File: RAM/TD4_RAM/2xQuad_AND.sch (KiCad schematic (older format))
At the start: 2 parts, among them U4 74HC21

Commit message: RAM done (damn buses\!)
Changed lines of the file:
@@
 $Descr A4 11693 8268
 encoding utf-8
-Sheet 5 46
+Sheet 5 47
 Title ""
 Date ""
@@
 P 4950 2500
 AR Path="/5C5DC05E/5C84D72F/5C84D8AE" Ref="U4"  Part="1"
-AR Path="/5C5DC05E/5C8E8F76/5C84D8AE" Ref="U20"  Part="1"
-AR Path="/5C5DC05E/5C8E8F7D/5C84D8AE" Ref="U21"  Part="1"
-AR Path="/5C5DC05E/5C8E8F84/5C84D8AE" Ref="U29"  Part="1"
-AR Path="/5C5DC05E/5C8E8FA2/5C84D8AE" Ref="U28"  Part="1"
-AR Path="/5C5DC05E/5C8E8FA8/5C84D8AE" Ref="U22"  Part="1"
-AR Path="/5C5DC05E/5C8E8FAE/5C84D8AE" Ref="U23"  Part="1"
-AR Path="/5C5DC05E/5C8E8FB4/5C84D8AE" Ref="U24"  Part="1"
-F 0 "U29" H 4950 2875 50  0000 C CNN
+AR Path="/5C5DC05E/5C8E8F76/5C84D8AE" Ref="U?"  Part="1"
+AR Path="/5C5DC05E/5C8E8F7D/5C84D8AE" Ref="U?"  Part="1"
+AR Path="/5C5DC05E/5C8E8F84/5C84D8AE" Ref="U?"  Part="1"
+AR Path="/5C5DC05E/5C8E8FA2/5C84D8AE" Ref="U?"  Part="1"
+AR Path="/5C5DC05E/5C8E8FA8/5C84D8AE" Ref="U?"  Part="1"
+AR Path="/5C5DC05E/5C8E8FAE/5C84D8AE" Ref="U?"  Part="1"
+AR Path="/5C5DC05E/5C8E8FB4/5C84D8AE" Ref="U?"  Part="1"
+AR Path="/5C5DC05E/5CD2847D/5C84D8AE" Ref="U35"  Part="1"
+AR Path="/5C5DC05E/5CD2F166/5C84D8AE" Ref="U36"  Part="1"
+AR Path="/5C5DC05E/5CD35E4F/5C84D8AE" Ref="U37"  Part="1"
+AR Path="/5C5DC05E/5CD3CB4F/5C84D8AE" Ref="U38"  Part="1"
+AR Path="/5C5DC05E/5CD3CB55/5C84D8AE" Ref="U39"  Part="1"
+AR Path="/5C5DC05E/5CD3CB5B/5C84D8AE" Ref="U40"  Part="1"
+AR Path="/5C5DC05E/5CD3CB61/5C84D8AE" Ref="U41"  Part="1"
+F 0 "U4" H 4950 2875 50  0000 C CNN
 F 1 "74HC21" H 4950 2784 50  0000 C CNN
 F 2 "" H 4950 2500 50  0001 C CNN
@@
 P 4950 3550
 AR Path="/5C5DC05E/5C84D72F/5C84D8EE" Ref="U4"  Part="2"
-AR Path="/5C5DC05E/5C8E8F76/5C84D8EE" Ref="U20"  Part="2"
-AR Path="/5C5DC05E/5C8E8F7D/5C84D8EE" Ref="U21"  Part="2"
-AR Path="/5C5DC05E/5C8E8F84/5C84D8EE" Ref="U29"  Part="2"
-AR Path="/5C5DC05E/5C8E8FA2/5C84D8EE" Ref="U28"  Part="2"
-AR Path="/5C5DC05E/5C8E8FA8/5C84D8EE" Ref="U22"  Part="2"
-AR Path="/5C5DC05E/5C8E8FAE/5C84D8EE" Ref="U23"  Part="2"
-AR Path="/5C5DC05E/5C8E8FB4/5C84D8EE" Ref="U24"  Part="2"
-F 0 "U29" H 4950 3925 50  0000 C CNN
+AR Path="/5C5DC05E/5C8E8F76/5C84D8EE" Ref="U?"  Part="2"
+AR Path="/5C5DC05E/5C8E8F7D/5C84D8EE" Ref="U?"  Part="2"
+AR Path="/5C5DC05E/5C8E8F84/5C84D8EE" Ref="U?"  Part="2"
+AR Path="/5C5DC05E/5C8E8FA2/5C84D8EE" Ref="U?"  Part="2"
+AR Path="/5C5DC05E/5C8E8FA8/5C84D8EE" Ref="U?"  Part="2"
+AR Path="/5C5DC05E/5C8E8FAE/5C84D8EE" Ref="U?"  Part="2"
+AR Path="/5C5DC05E/5C8E8FB4/5C84D8EE" Ref="U?"  Part="2"
+AR Path="/5C5DC05E/5CD2847D/5C84D8EE" Ref="U35"  Part="2"
+AR Path="/5C5DC05E/5CD2F166/5C84D8EE" Ref="U36"  Part="2"
+AR Path="/5C5DC05E/5CD35E4F/5C84D8EE" Ref="U37"  Part="2"
+AR Path="/5C5DC05E/5CD3CB4F/5C84D8EE" Ref="U38"  Part="2"
+AR Path="/5C5DC05E/5CD3CB55/5C84D8EE" Ref="U39"  Part="2"
+AR Path="/5C5DC05E/5CD3CB5B/5C84D8EE" Ref="U40"  Part="2"
+AR Path="/5C5DC05E/5CD3CB61/5C84D8EE" Ref="U41"  Part="2"
+F 0 "U4" H 4950 3925 50  0000 C CNN
 F 1 "74HC21" H 4950 3834 50  0000 C CNN
 F 2 "" H 4950 3550 50  0001 C CNN
@@
 P 8050 5500
 AR Path="/5C5DC05E/5C84D72F/5C84D959" Ref="U4"  Part="3"
-AR Path="/5C5DC05E/5C8E8F76/5C84D959" Ref="U20"  Part="3"
-AR Path="/5C5DC05E/5C8E8F7D/5C84D959" Ref="U21"  Part="3"
-AR Path="/5C5DC05E/5C8E8F84/5C84D959" Ref="U29"  Part="3"
-AR Path="/5C5DC05E/5C8E8FA2/5C84D959" Ref="U28"  Part="3"
-AR Path="/5C5DC05E/5C8E8FA8/5C84D959" Ref="U22"  Part="3"
-AR Path="/5C5DC05E/5C8E8FAE/5C84D959" Ref="U23"  Part="3"
-AR Path="/5C5DC05E/5C8E8FB4/5C84D959" Ref="U24"  Part="3"
-F 0 "U29" H 8280 5546 50  0000 L CNN
+AR Path="/5C5DC05E/5C8E8F76/5C84D959" Ref="U?"  Part="3"
+AR Path="/5C5DC05E/5C8E8F7D/5C84D959" Ref="U?"  Part="3"
+AR Path="/5C5DC05E/5C8E8F84/5C84D959" Ref="U?"  Part="3"
+AR Path="/5C5DC05E/5C8E8FA2/5C84D959" Ref="U?"  Part="3"
+AR Path="/5C5DC05E/5C8E8FA8/5C84D959" Ref="U?"  Part="3"
+AR Path="/5C5DC05E/5C8E8FAE/5C84D959" Ref="U?"  Part="3"
+AR Path="/5C5DC05E/5C8E8FB4/5C84D959" Ref="U?"  Part="3"
+AR Path="/5C5DC05E/5CD2847D/5C84D959" Ref="U35"  Part="3"
+AR Path="/5C5DC05E/5CD2F166/5C84D959" Ref="U36"  Part="3"
+AR Path="/5C5DC05E/5CD35E4F/5C84D959" Ref="U37"  Part="3"
+AR Path="/5C5DC05E/5CD3CB4F/5C84D959" Ref="U38"  Part="3"
+AR Path="/5C5DC05E/5CD3CB55/5C84D959" Ref="U39"  Part="3"
+AR Path="/5C5DC05E/5CD3CB5B/5C84D959" Ref="U40"  Part="3"
+AR Path="/5C5DC05E/5CD3CB61/5C84D959" Ref="U41"  Part="3"
+F 0 "U4" H 8280 5546 50  0000 L CNN
 F 1 "74HC21" H 8280 5455 50  0000 L CNN
 F 2 "" H 8050 5500 50  0001 C CNN
@@
 P 8700 5500
 AR Path="/5C5DC05E/5C84D72F/5C84DA33" Ref="C3"  Part="1"
-AR Path="/5C5DC05E/5C8E8F76/5C84DA33" Ref="C19"  Part="1"
-AR Path="/5C5DC05E/5C8E8F7D/5C84DA33" Ref="C20"  Part="1"
-AR Path="/5C5DC05E/5C8E8F84/5C84DA33" Ref="C28"  Part="1"
-AR Path="/5C5DC05E/5C8E8FA2/5C84DA33" Ref="C27"  Part="1"
-AR Path="/5C5DC05E/5C8E8FA8/5C84DA33" Ref="C21"  Part="1"
-AR Path="/5C5DC05E/5C8E8FAE/5C84DA33" Ref="C22"  Part="1"
-AR Path="/5C5DC05E/5C8E8FB4/5C84DA33" Ref="C23"  Part="1"
-F 0 "C28" H 8815 5546 50  0000 L CNN
+AR Path="/5C5DC05E/5C8E8F76/5C84DA33" Ref="C?"  Part="1"
+AR Path="/5C5DC05E/5C8E8F7D/5C84DA33" Ref="C?"  Part="1"
+AR Path="/5C5DC05E/5C8E8F84/5C84DA33" Ref="C?"  Part="1"
+AR Path="/5C5DC05E/5C8E8FA2/5C84DA33" Ref="C?"  Part="1"
+AR Path="/5C5DC05E/5C8E8FA8/5C84DA33" Ref="C?"  Part="1"
+AR Path="/5C5DC05E/5C8E8FAE/5C84DA33" Ref="C?"  Part="1"
+AR Path="/5C5DC05E/5C8E8FB4/5C84DA33" Ref="C?"  Part="1"
+AR Path="/5C5DC05E/5CD2847D/5C84DA33" Ref="C34"  Part="1"
+AR Path="/5C5DC05E/5CD2F166/5C84DA33" Ref="C35"  Part="1"
+AR Path="/5C5DC05E/5CD35E4F/5C84DA33" Ref="C36"  Part="1"
+AR Path="/5C5DC05E/5CD3CB4F/5C84DA33" Ref="C37"  Part="1"
+AR Path="/5C5DC05E/5CD3CB55/5C84DA33" Ref="C38"  Part="1"
+AR Path="/5C5DC05E/5CD3CB5B/5C84DA33" Ref="C39"  Part="1"
+AR Path="/5C5DC05E/5CD3CB61/5C84DA33" Ref="C40"  Part="1"
+F 0 "C3" H 8815 5546 50  0000 L CNN
 F 1 "100n" H 8815 5455 50  0000 L CNN
 F 2 "" H 8738 5350 50  0001 C CNN
@@
 	8700 5650 8700 6100
 $Comp
-L power:GND #PWR012
+L power:GND #PWR010
 U 1 1 5C84DB98
 P 8400 6100
-AR Path="/5C5DC05E/5C84D72F/5C84DB98" Ref="#PWR012"  Part="1"
-AR Path="/5C5DC05E/5C8E8F76/5C84DB98" Ref="#PWR074"  Part="1"
-AR Path="/5C5DC05E/5C8E8F7D/5C84DB98" Ref="#PWR076"  Part="1"
-AR Path="/5C5DC05E/5C8E8F84/5C84DB98" Ref="#PWR089"  Part="1"
-AR Path="/5C5DC05E/5C8E8FA2/5C84DB98" Ref="#PWR087"  Part="1"
-AR Path="/5C5DC05E/5C8E8FA8/5C84DB98" Ref="#PWR078"  Part="1"
-AR Path="/5C5DC05E/5C8E8FAE/5C84DB98" Ref="#PWR080"  Part="1"
-AR Path="/5C5DC05E/5C8E8FB4/5C84DB98" Ref="#PWR082"  Part="1"
-F 0 "#PWR089" H 8400 5850 50  0001 C CNN
+AR Path="/5C5DC05E/5C84D72F/5C84DB98" Ref="#PWR010"  Part="1"
+AR Path="/5C5DC05E/5C8E8F76/5C84DB98" Ref="#PWR?"  Part="1"
+AR Path="/5C5DC05E/5C8E8F7D/5C84DB98" Ref="#PWR?"  Part="1"
+AR Path="/5C5DC05E/5C8E8F84/5C84DB98" Ref="#PWR?"  Part="1"
+AR Path="/5C5DC05E/5C8E8FA2/5C84DB98" Ref="#PWR?"  Part="1"
+AR Path="/5C5DC05E/5C8E8FA8/5C84DB98" Ref="#PWR?"  Part="1"
+AR Path="/5C5DC05E/5C8E8FAE/5C84DB98" Ref="#PWR?"  Part="1"
+AR Path="/5C5DC05E/5C8E8FB4/5C84DB98" Ref="#PWR?"  Part="1"
+AR Path="/5C5DC05E/5CD2847D/5C84DB98" Ref="#PWR0132"  Part="1"
+AR Path="/5C5DC05E/5CD2F166/5C84DB98" Ref="#PWR0134"  Part="1"
+AR Path="/5C5DC05E/5CD35E4F/5C84DB98" Ref="#PWR0136"  Part="1"
+AR Path="/5C5DC05E/5CD3CB4F/5C84DB98" Ref="#PWR0138"  Part="1"
+AR Path="/5C5DC05E/5CD3CB55/5C84DB98" Ref="#PWR0140"  Part="1"
+AR Path="/5C5DC05E/5CD3CB5B/5C84DB98" Ref="#PWR0142"  Part="1"
+AR Path="/5C5DC05E/5CD3CB61/5C84DB98" Ref="#PWR0144"  Part="1"
+F 0 "#PWR0144" H 8400 5850 50  0001 C CNN
 F 1 "GND" H 8405 5927 50  0000 C CNN
 F 2 "" H 8400 6100 50  0001 C CNN
@@
 	8400 6100 8700 6100
 $Comp
-L power:VCC #PWR011
+L power:VCC #PWR09
 U 1 1 5C84DC2A
 P 8400 4900
-AR Path="/5C5DC05E/5C84D72F/5C84DC2A" Ref="#PWR011"  Part="1"
-AR Path="/5C5DC05E/5C8E8F76/5C84DC2A" Ref="#PWR073"  Part="1"
-AR Path="/5C5DC05E/5C8E8F7D/5C84DC2A" Ref="#PWR075"  Part="1"
-AR Path="/5C5DC05E/5C8E8F84/5C84DC2A" Ref="#PWR088"  Part="1"
-AR Path="/5C5DC05E/5C8E8FA2/5C84DC2A" Ref="#PWR086"  Part="1"
-AR Path="/5C5DC05E/5C8E8FA8/5C84DC2A" Ref="#PWR077"  Part="1"
-AR Path="/5C5DC05E/5C8E8FAE/5C84DC2A" Ref="#PWR079"  Part="1"
-AR Path="/5C5DC05E/5C8E8FB4/5C84DC2A" Ref="#PWR081"  Part="1"
-F 0 "#PWR088" H 8400 4750 50  0001 C CNN
+AR Path="/5C5DC05E/5C84D72F/5C84DC2A" Ref="#PWR09"  Part="1"
+AR Path="/5C5DC05E/5C8E8F76/5C84DC2A" Ref="#PWR?"  Part="1"
+AR Path="/5C5DC05E/5C8E8F7D/5C84DC2A" Ref="#PWR?"  Part="1"
+AR Path="/5C5DC05E/5C8E8F84/5C84DC2A" Ref="#PWR?"  Part="1"
+AR Path="/5C5DC05E/5C8E8FA2/5C84DC2A" Ref="#PWR?"  Part="1"
+AR Path="/5C5DC05E/5C8E8FA8/5C84DC2A" Ref="#PWR?"  Part="1"
+AR Path="/5C5DC05E/5C8E8FAE/5C84DC2A" Ref="#PWR?"  Part="1"
+AR Path="/5C5DC05E/5C8E8FB4/5C84DC2A" Ref="#PWR?"  Part="1"
+AR Path="/5C5DC05E/5CD2847D/5C84DC2A" Ref="#PWR0131"  Part="1"
+AR Path="/5C5DC05E/5CD2F166/5C84DC2A" Ref="#PWR0133"  Part="1"
+AR Path="/5C5DC05E/5CD35E4F/5C84DC2A" Ref="#PWR0135"  Part="1"
+AR Path="/5C5DC05E/5CD3CB4F/5C84DC2A" Ref="#PWR0137"  Part="1"
+AR Path="/5C5DC05E/5CD3CB55/5C84DC2A" Ref="#PWR0139"  Part="1"
+AR Path="/5C5DC05E/5CD3CB5B/5C84DC2A" Ref="#PWR0141"  Part="1"
+AR Path="/5C5DC05E/5CD3CB61/5C84DC2A" Ref="#PWR0143"  Part="1"
+F 0 "#PWR0143" H 8400 4750 50  0001 C CNN
 F 1 "VCC" H 8417 5073 50  0000 C CNN
 F 2 "" H 8400 4900 50  0001 C CNN
@@
 Text Label 3900 3150 0    50   ~ 0
 B[0..3]
-Wire Bus Line
-	4450 2100 4450 2550
-Wire Bus Line
-	4450 3150 4450 3600
 Text Label 4550 3400 0    50   ~ 0
 B0
@@
 B3
 Text HLabel 3800 2100 0    50   Input ~ 0
-A
+A[0..3]
 Text HLabel 3800 3150 0    50   Input ~ 0
-B
+B[0..3]
+Wire Bus Line
+	4450 2100 4450 2550
+Wire Bus Line
+	4450 3150 4450 3600
 $EndSCHEMATC

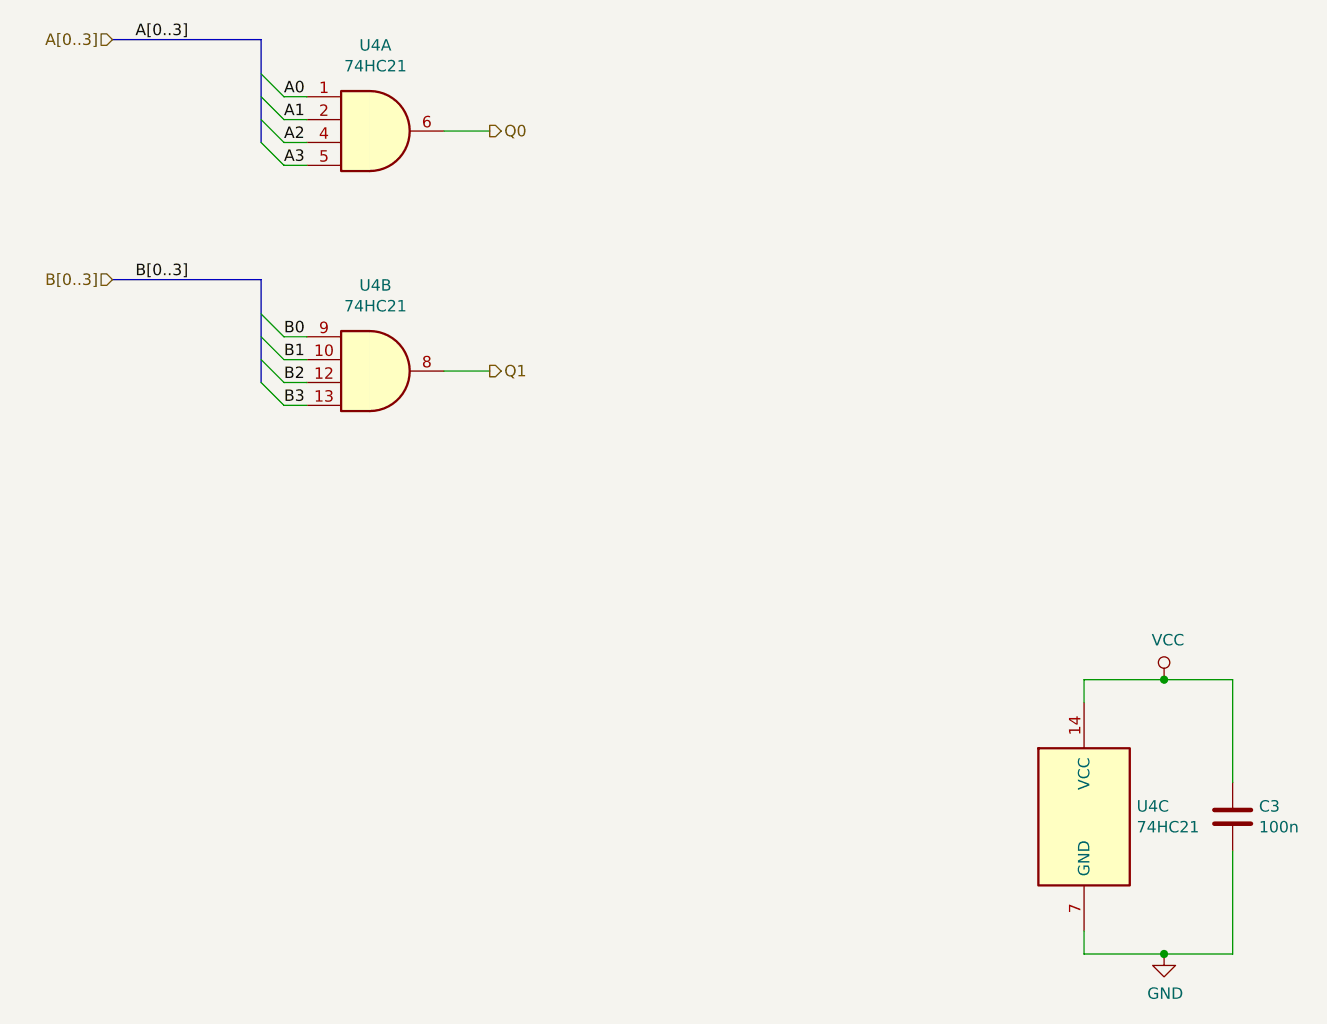
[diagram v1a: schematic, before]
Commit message: Added backplane connectors to all PCBs
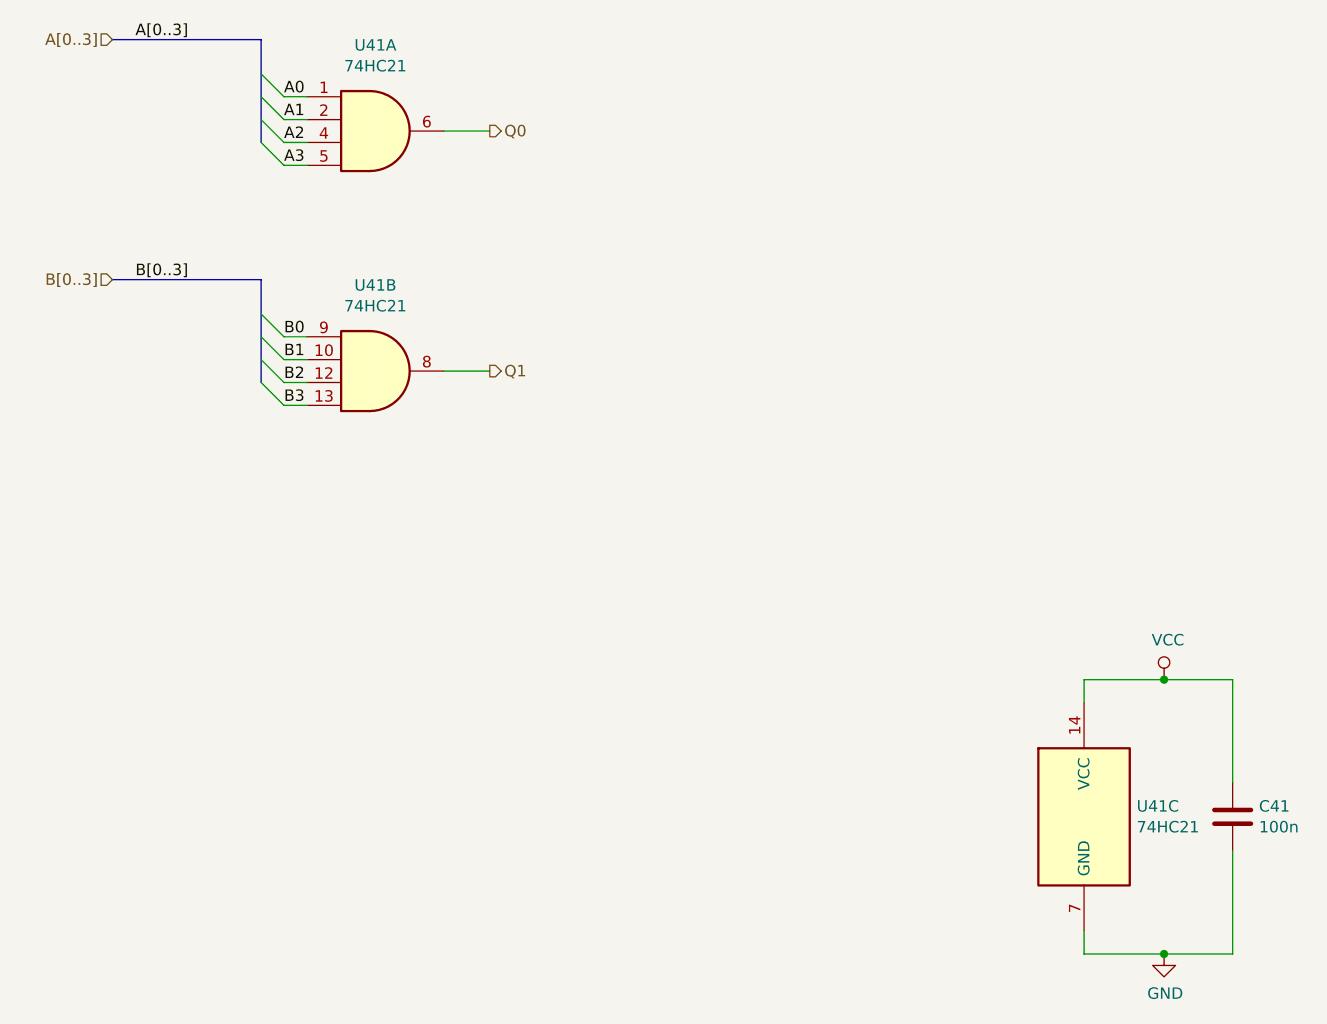
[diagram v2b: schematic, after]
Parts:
- C4: renamed from C3; footprint (none) -> Capacitor_SMD:C_0805_2012Metric
- U4: footprint (none) -> Package_SO:SOIC-14_3.9x8.7mm_P1.27mm
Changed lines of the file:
@@
 AR Path="/5C5DC05E/5CD3CB5B/5C84D8AE" Ref="U40"  Part="1"
 AR Path="/5C5DC05E/5CD3CB61/5C84D8AE" Ref="U41"  Part="1"
-F 0 "U4" H 4950 2875 50  0000 C CNN
+F 0 "U41" H 4950 2875 50  0000 C CNN
 F 1 "74HC21" H 4950 2784 50  0000 C CNN
-F 2 "" H 4950 2500 50  0001 C CNN
+F 2 "Package_SO:SOIC-14_3.9x8.7mm_P1.27mm" H 4950 2500 50  0001 C CNN
 F 3 "http://www.ti.com/lit/gpn/sn74LS21" H 4950 2500 50  0001 C CNN
 	1    4950 2500
@@
 AR Path="/5C5DC05E/5CD3CB5B/5C84D8EE" Ref="U40"  Part="2"
 AR Path="/5C5DC05E/5CD3CB61/5C84D8EE" Ref="U41"  Part="2"
-F 0 "U4" H 4950 3925 50  0000 C CNN
+F 0 "U41" H 4950 3925 50  0000 C CNN
 F 1 "74HC21" H 4950 3834 50  0000 C CNN
-F 2 "" H 4950 3550 50  0001 C CNN
+F 2 "Package_SO:SOIC-14_3.9x8.7mm_P1.27mm" H 4950 3550 50  0001 C CNN
 F 3 "http://www.ti.com/lit/gpn/sn74LS21" H 4950 3550 50  0001 C CNN
 	2    4950 3550
@@
 AR Path="/5C5DC05E/5CD3CB5B/5C84D959" Ref="U40"  Part="3"
 AR Path="/5C5DC05E/5CD3CB61/5C84D959" Ref="U41"  Part="3"
-F 0 "U4" H 8280 5546 50  0000 L CNN
+F 0 "U41" H 8280 5546 50  0000 L CNN
 F 1 "74HC21" H 8280 5455 50  0000 L CNN
-F 2 "" H 8050 5500 50  0001 C CNN
+F 2 "Package_SO:SOIC-14_3.9x8.7mm_P1.27mm" H 8050 5500 50  0001 C CNN
 F 3 "http://www.ti.com/lit/gpn/sn74LS21" H 8050 5500 50  0001 C CNN
 	3    8050 5500
@@
 $EndComp
 $Comp
-L Device:C C3
+L Device:C C4
 U 1 1 5C84DA33
 P 8700 5500
-AR Path="/5C5DC05E/5C84D72F/5C84DA33" Ref="C3"  Part="1"
+AR Path="/5C5DC05E/5C84D72F/5C84DA33" Ref="C4"  Part="1"
 AR Path="/5C5DC05E/5C8E8F76/5C84DA33" Ref="C?"  Part="1"
 AR Path="/5C5DC05E/5C8E8F7D/5C84DA33" Ref="C?"  Part="1"
@@
 AR Path="/5C5DC05E/5C8E8FAE/5C84DA33" Ref="C?"  Part="1"
 AR Path="/5C5DC05E/5C8E8FB4/5C84DA33" Ref="C?"  Part="1"
-AR Path="/5C5DC05E/5CD2847D/5C84DA33" Ref="C34"  Part="1"
-AR Path="/5C5DC05E/5CD2F166/5C84DA33" Ref="C35"  Part="1"
-AR Path="/5C5DC05E/5CD35E4F/5C84DA33" Ref="C36"  Part="1"
-AR Path="/5C5DC05E/5CD3CB4F/5C84DA33" Ref="C37"  Part="1"
-AR Path="/5C5DC05E/5CD3CB55/5C84DA33" Ref="C38"  Part="1"
-AR Path="/5C5DC05E/5CD3CB5B/5C84DA33" Ref="C39"  Part="1"
-AR Path="/5C5DC05E/5CD3CB61/5C84DA33" Ref="C40"  Part="1"
-F 0 "C3" H 8815 5546 50  0000 L CNN
+AR Path="/5C5DC05E/5CD2847D/5C84DA33" Ref="C35"  Part="1"
+AR Path="/5C5DC05E/5CD2F166/5C84DA33" Ref="C36"  Part="1"
+AR Path="/5C5DC05E/5CD35E4F/5C84DA33" Ref="C37"  Part="1"
+AR Path="/5C5DC05E/5CD3CB4F/5C84DA33" Ref="C38"  Part="1"
+AR Path="/5C5DC05E/5CD3CB55/5C84DA33" Ref="C39"  Part="1"
+AR Path="/5C5DC05E/5CD3CB5B/5C84DA33" Ref="C40"  Part="1"
+AR Path="/5C5DC05E/5CD3CB61/5C84DA33" Ref="C41"  Part="1"
+F 0 "C41" H 8815 5546 50  0000 L CNN
 F 1 "100n" H 8815 5455 50  0000 L CNN
-F 2 "" H 8738 5350 50  0001 C CNN
+F 2 "Capacitor_SMD:C_0805_2012Metric" H 8738 5350 50  0001 C CNN
 F 3 "~" H 8700 5500 50  0001 C CNN
 	1    8700 5500
@@
 	8700 5650 8700 6100
 $Comp
-L power:GND #PWR010
+L power:GND #PWR025
 U 1 1 5C84DB98
 P 8400 6100
-AR Path="/5C5DC05E/5C84D72F/5C84DB98" Ref="#PWR010"  Part="1"
+AR Path="/5C5DC05E/5C84D72F/5C84DB98" Ref="#PWR025"  Part="1"
 AR Path="/5C5DC05E/5C8E8F76/5C84DB98" Ref="#PWR?"  Part="1"
 AR Path="/5C5DC05E/5C8E8F7D/5C84DB98" Ref="#PWR?"  Part="1"
@@
 AR Path="/5C5DC05E/5C8E8FAE/5C84DB98" Ref="#PWR?"  Part="1"
 AR Path="/5C5DC05E/5C8E8FB4/5C84DB98" Ref="#PWR?"  Part="1"
-AR Path="/5C5DC05E/5CD2847D/5C84DB98" Ref="#PWR0132"  Part="1"
-AR Path="/5C5DC05E/5CD2F166/5C84DB98" Ref="#PWR0134"  Part="1"
-AR Path="/5C5DC05E/5CD35E4F/5C84DB98" Ref="#PWR0136"  Part="1"
-AR Path="/5C5DC05E/5CD3CB4F/5C84DB98" Ref="#PWR0138"  Part="1"
-AR Path="/5C5DC05E/5CD3CB55/5C84DB98" Ref="#PWR0140"  Part="1"
-AR Path="/5C5DC05E/5CD3CB5B/5C84DB98" Ref="#PWR0142"  Part="1"
-AR Path="/5C5DC05E/5CD3CB61/5C84DB98" Ref="#PWR0144"  Part="1"
-F 0 "#PWR0144" H 8400 5850 50  0001 C CNN
+AR Path="/5C5DC05E/5CD2847D/5C84DB98" Ref="#PWR0147"  Part="1"
+AR Path="/5C5DC05E/5CD2F166/5C84DB98" Ref="#PWR0149"  Part="1"
+AR Path="/5C5DC05E/5CD35E4F/5C84DB98" Ref="#PWR0151"  Part="1"
+AR Path="/5C5DC05E/5CD3CB4F/5C84DB98" Ref="#PWR0153"  Part="1"
+AR Path="/5C5DC05E/5CD3CB55/5C84DB98" Ref="#PWR0155"  Part="1"
+AR Path="/5C5DC05E/5CD3CB5B/5C84DB98" Ref="#PWR0157"  Part="1"
+AR Path="/5C5DC05E/5CD3CB61/5C84DB98" Ref="#PWR0159"  Part="1"
+F 0 "#PWR0159" H 8400 5850 50  0001 C CNN
 F 1 "GND" H 8405 5927 50  0000 C CNN
 F 2 "" H 8400 6100 50  0001 C CNN
@@
 	8400 6100 8700 6100
 $Comp
-L power:VCC #PWR09
+L power:VCC #PWR024
 U 1 1 5C84DC2A
 P 8400 4900
-AR Path="/5C5DC05E/5C84D72F/5C84DC2A" Ref="#PWR09"  Part="1"
+AR Path="/5C5DC05E/5C84D72F/5C84DC2A" Ref="#PWR024"  Part="1"
 AR Path="/5C5DC05E/5C8E8F76/5C84DC2A" Ref="#PWR?"  Part="1"
 AR Path="/5C5DC05E/5C8E8F7D/5C84DC2A" Ref="#PWR?"  Part="1"
@@
 AR Path="/5C5DC05E/5C8E8FAE/5C84DC2A" Ref="#PWR?"  Part="1"
 AR Path="/5C5DC05E/5C8E8FB4/5C84DC2A" Ref="#PWR?"  Part="1"
-AR Path="/5C5DC05E/5CD2847D/5C84DC2A" Ref="#PWR0131"  Part="1"
-AR Path="/5C5DC05E/5CD2F166/5C84DC2A" Ref="#PWR0133"  Part="1"
-AR Path="/5C5DC05E/5CD35E4F/5C84DC2A" Ref="#PWR0135"  Part="1"
-AR Path="/5C5DC05E/5CD3CB4F/5C84DC2A" Ref="#PWR0137"  Part="1"
-AR Path="/5C5DC05E/5CD3CB55/5C84DC2A" Ref="#PWR0139"  Part="1"
-AR Path="/5C5DC05E/5CD3CB5B/5C84DC2A" Ref="#PWR0141"  Part="1"
-AR Path="/5C5DC05E/5CD3CB61/5C84DC2A" Ref="#PWR0143"  Part="1"
-F 0 "#PWR0143" H 8400 4750 50  0001 C CNN
+AR Path="/5C5DC05E/5CD2847D/5C84DC2A" Ref="#PWR0146"  Part="1"
+AR Path="/5C5DC05E/5CD2F166/5C84DC2A" Ref="#PWR0148"  Part="1"
+AR Path="/5C5DC05E/5CD35E4F/5C84DC2A" Ref="#PWR0150"  Part="1"
+AR Path="/5C5DC05E/5CD3CB4F/5C84DC2A" Ref="#PWR0152"  Part="1"
+AR Path="/5C5DC05E/5CD3CB55/5C84DC2A" Ref="#PWR0154"  Part="1"
+AR Path="/5C5DC05E/5CD3CB5B/5C84DC2A" Ref="#PWR0156"  Part="1"
+AR Path="/5C5DC05E/5CD3CB61/5C84DC2A" Ref="#PWR0158"  Part="1"
+F 0 "#PWR0158" H 8400 4750 50  0001 C CNN
 F 1 "VCC" H 8417 5073 50  0000 C CNN
 F 2 "" H 8400 4900 50  0001 C CNN
